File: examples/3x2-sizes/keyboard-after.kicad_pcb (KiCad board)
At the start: 2 copper layers, 63.6 x 50.8 mm, 11 parts, among them SW1 SW_Push, SW2 SW_Push, SW3 SW_Push, SW4 SW_Push, SW5 SW_Push

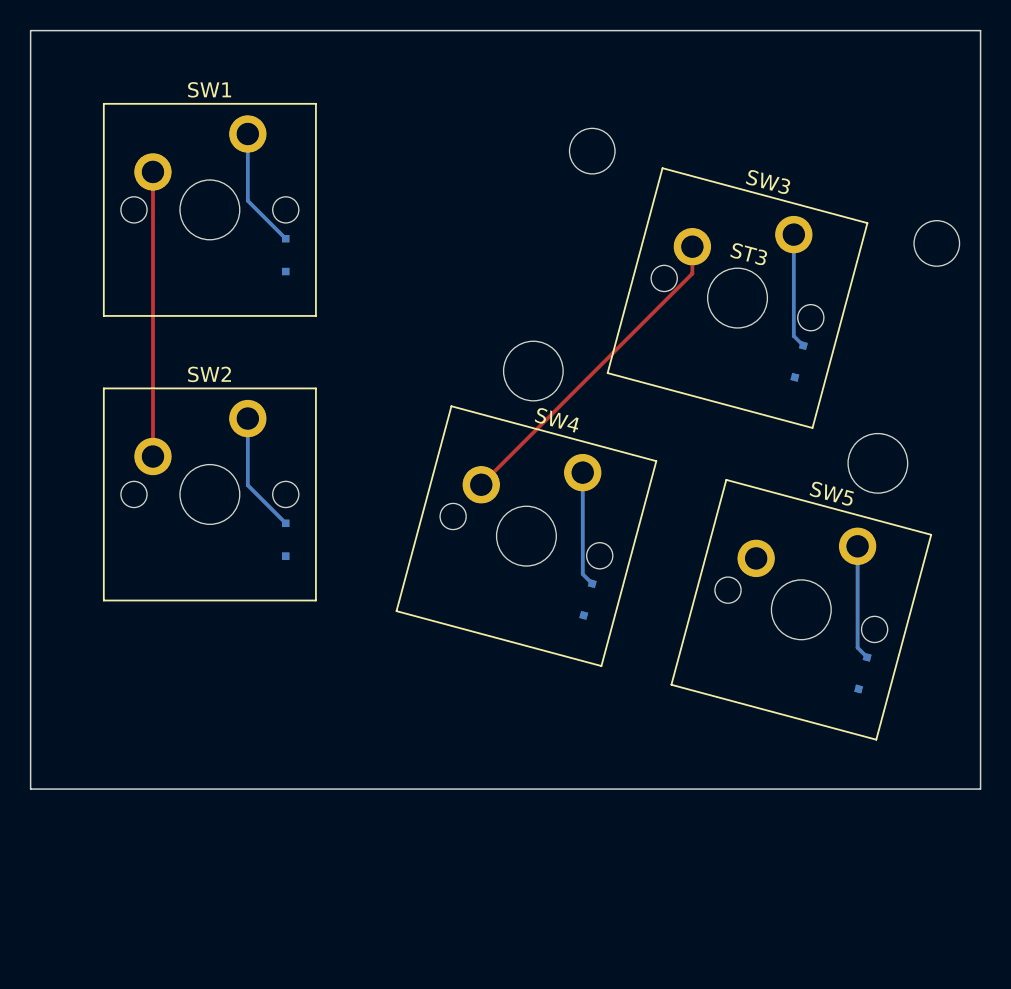
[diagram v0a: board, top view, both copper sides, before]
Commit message: examples result update
also simplified example filenames and add new example
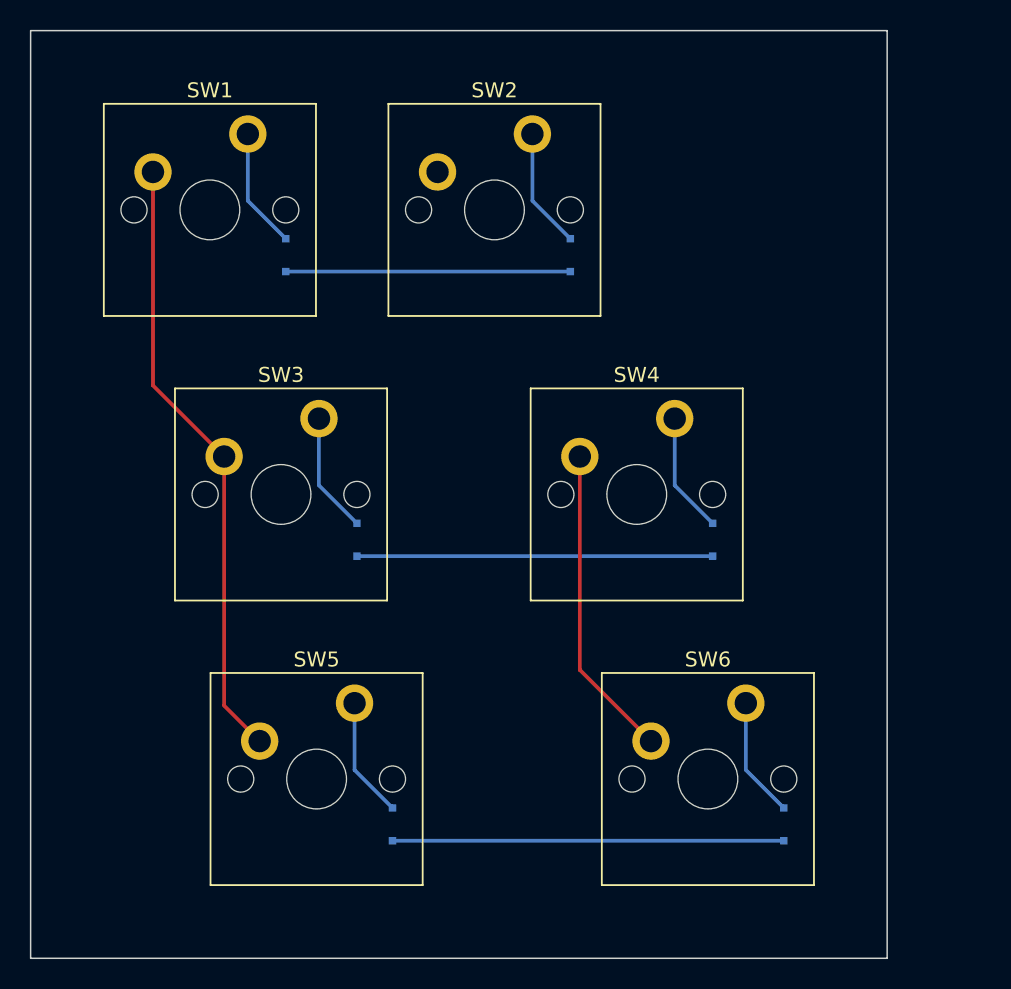
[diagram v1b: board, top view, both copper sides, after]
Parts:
- removed ST3: MountingHole, Stabilizer_Cherry_MX_2u
- added D6: D, D_SOD-323F, B.Cu at (72.9, 75.7)
- added SW6: SW_Push, SW_Cherry_MX_PCB_1.00u, F.Cu at (67.9, 72.6)
- SW3: footprint SW_Cherry_MX_PCB_2.00u -> SW_Cherry_MX_PCB_1.50u
- SW5: footprint SW_Cherry_MX_PCB_1.00u -> SW_Cherry_MX_PCB_1.75u
- moved SW5 34.4 mm to (41.7, 72.6), turned to 0 degrees
- moved SW3 33.3 mm to (39.3, 53.6), turned to 0 degrees
- moved D5 33.1 mm to (46.7, 75.7), turned to 90 degrees
- moved D3 31.9 mm to (44.4, 56.6), turned to 90 degrees
- moved SW2 26.9 mm to (53.6, 34.5)
- moved D2 26.9 mm to (58.7, 37.6)
- moved D4 9.25 mm to (68.2, 56.6), turned to 90 degrees
- moved SW4 7.89 mm to (63.1, 53.6), turned to 0 degrees
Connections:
- D2 pad 1: ROW1 -> ROW0
- D3 pad 1: ROW0 -> ROW1
- D5 pad 1: ROW1 -> ROW2
- SW2 pad 1: COL0 -> COL1
- SW3 pad 1: COL1 -> COL0
- SW4 pad 1: COL1 -> COL2
- SW5 pad 1: COL2 -> COL0
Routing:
- net ROW2: track 0.00 -> 26.2 mm
- net ROW1: track 0.00 -> 23.8 mm
- net COL0: track 19.0 -> 41.1 mm
- net COL1: track 21.8 -> 0.00 mm
- net COL2: track 0.00 -> 21.0 mm
- net ROW0: track 0.00 -> 19.1 mm
- net N$6: track 0.00 -> 8.06 mm
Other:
- board size 63.6 x 50.8 mm -> 57.3 x 62.1 mm

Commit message: Update examples kicad files
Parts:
- D1, D2, D3, D4, D5, D6: footprint D_SOD-323F -> Diode_SMD:D_SOD-323F
- SW1, SW2, SW4, SW6: footprint SW_Cherry_MX_PCB_1.00u -> Switch_Keyboard_Cherry_MX:SW_Cherry_MX_PCB_1.00u
- SW3: footprint SW_Cherry_MX_PCB_1.50u -> Switch_Keyboard_Cherry_MX:SW_Cherry_MX_PCB_1.50u
- SW5: footprint SW_Cherry_MX_PCB_1.75u -> Switch_Keyboard_Cherry_MX:SW_Cherry_MX_PCB_1.75u
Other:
- board outline removed
- net class Default removed

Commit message: Maintain own copy of footprints used in examples
Because testing with more footprints variants will be added soon,
it would be easier to maintain own copy of used footprints than
include multiple submodules for various libraries.
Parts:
- SW1, SW2, SW4, SW6: footprint Switch_Keyboard_Cherry_MX:SW_Cherry_MX_PCB_1.00u -> examples:SW_Cherry_MX_PCB_1.00u
- SW3: footprint Switch_Keyboard_Cherry_MX:SW_Cherry_MX_PCB_1.50u -> examples:SW_Cherry_MX_PCB_1.50u
- SW5: footprint Switch_Keyboard_Cherry_MX:SW_Cherry_MX_PCB_1.75u -> examples:SW_Cherry_MX_PCB_1.75u
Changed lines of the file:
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@@
   (net 11 "ROW1")
   (net 12 "ROW2")
-  (footprint "Switch_Keyboard_Cherry_MX:SW_Cherry_MX_PCB_1.00u" (layer "F.Cu")
+  (footprint "examples:SW_Cherry_MX_PCB_1.00u" (layer "F.Cu")
     (at 34.525 34.525)
     (descr "Cherry MX keyswitch, https://www.cherrymx.de/en/dev.html")
@@
     )
   )
-  (footprint "Switch_Keyboard_Cherry_MX:SW_Cherry_MX_PCB_1.00u" (layer "F.Cu")
+  (footprint "examples:SW_Cherry_MX_PCB_1.00u" (layer "F.Cu")
     (at 53.575 34.525)
     (descr "Cherry MX keyswitch, https://www.cherrymx.de/en/dev.html")
@@
     )
   )
-  (footprint "Switch_Keyboard_Cherry_MX:SW_Cherry_MX_PCB_1.50u" (layer "F.Cu")
+  (footprint "examples:SW_Cherry_MX_PCB_1.50u" (layer "F.Cu")
     (at 39.2875 53.575)
     (descr "Cherry MX keyswitch, https://www.cherrymx.de/en/dev.html")
@@
     )
   )
-  (footprint "Switch_Keyboard_Cherry_MX:SW_Cherry_MX_PCB_1.00u" (layer "F.Cu")
+  (footprint "examples:SW_Cherry_MX_PCB_1.00u" (layer "F.Cu")
     (at 63.1 53.575)
     (descr "Cherry MX keyswitch, https://www.cherrymx.de/en/dev.html")
@@
     )
   )
-  (footprint "Switch_Keyboard_Cherry_MX:SW_Cherry_MX_PCB_1.75u" (layer "F.Cu")
+  (footprint "examples:SW_Cherry_MX_PCB_1.75u" (layer "F.Cu")
     (at 41.66875 72.625)
     (descr "Cherry MX keyswitch, https://www.cherrymx.de/en/dev.html")
@@
     )
   )
-  (footprint "Switch_Keyboard_Cherry_MX:SW_Cherry_MX_PCB_1.00u" (layer "F.Cu")
+  (footprint "examples:SW_Cherry_MX_PCB_1.00u" (layer "F.Cu")
     (at 67.8625 72.625)
     (descr "Cherry MX keyswitch, https://www.cherrymx.de/en/dev.html")
